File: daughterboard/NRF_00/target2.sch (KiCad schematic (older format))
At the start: 4 parts

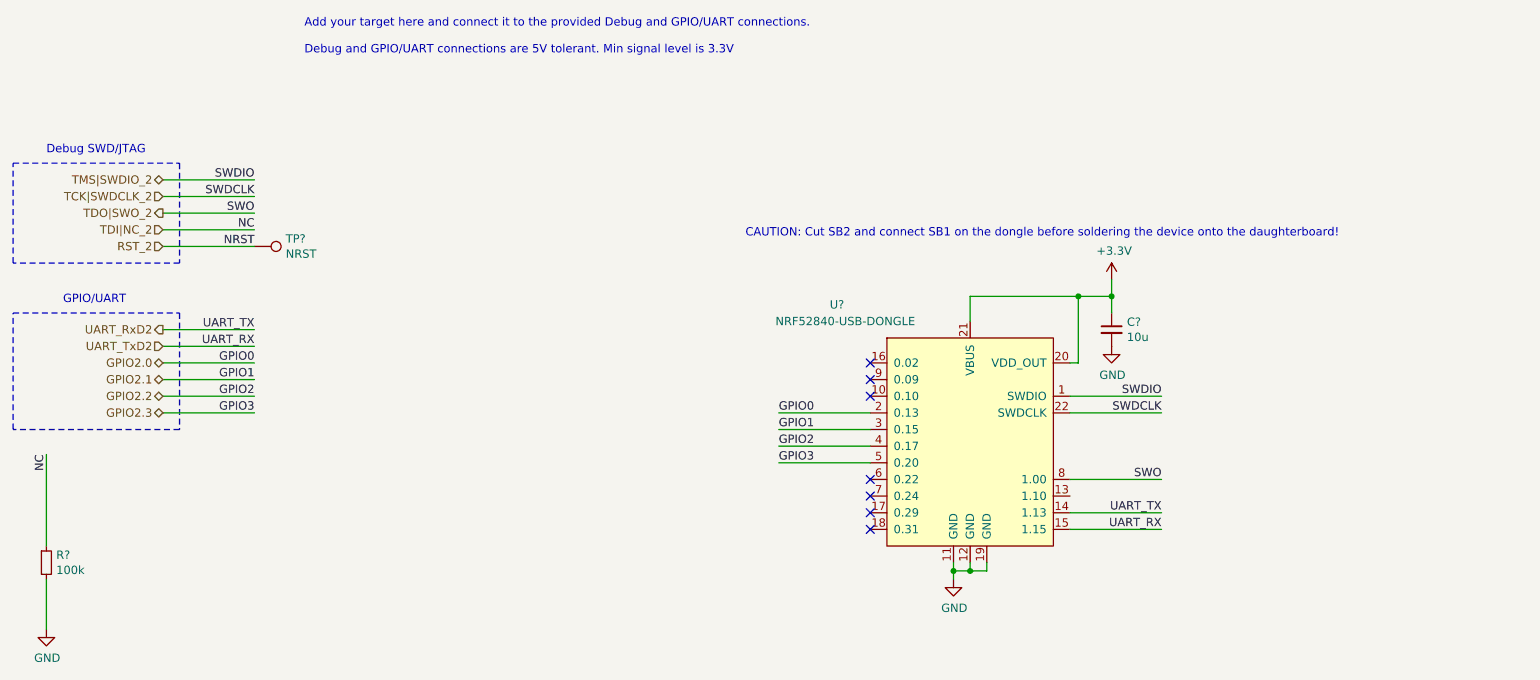
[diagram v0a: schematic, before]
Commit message: finished NRF daughterboard schematics
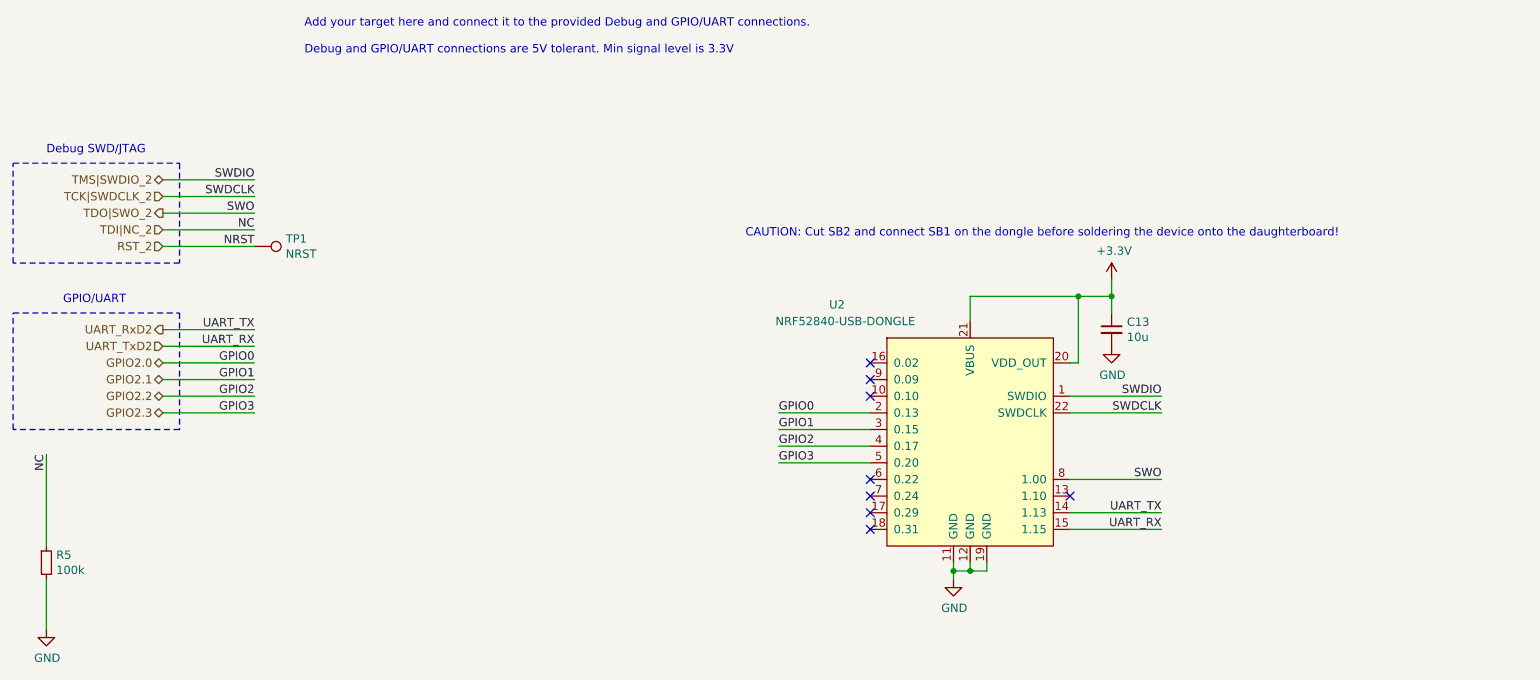
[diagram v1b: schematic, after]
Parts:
- gave numbers to parts that had none: 4
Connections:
- no-connect marks 7 -> 8
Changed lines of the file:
@@
 Add your target here and connect it to the provided Debug and GPIO/UART connections.\n\nDebug and GPIO/UART connections are 5V tolerant. Min signal level is 3.3V
 $Comp
-L hive_daughterboard:NRF52840-USB-DONGLE U?
+L hive_daughterboard:NRF52840-USB-DONGLE U2
 U 1 1 618F653D
 P 6500 2650
-F 0 "U?" H 5700 2850 50  0000 C CNN
+F 0 "U2" H 5700 2850 50  0000 C CNN
 F 1 "NRF52840-USB-DONGLE" H 5750 2750 50  0000 C CNN
 F 2 "hive_daughterboard:NRF52840-USB-DONGLE" H 6500 2650 50  0001 C CNN
@@
 	7150 2800 7100 2800
 $Comp
-L Device:C_Small C?
+L Device:C_Small C13
 U 1 1 618F9760
 P 7350 2600
-F 0 "C?" H 7442 2646 50  0000 L CNN
+F 0 "C13" H 7442 2646 50  0000 L CNN
 F 1 "10u" H 7442 2555 50  0000 L CNN
 F 2 "" H 7350 2600 50  0001 C CNN
@@
 Connection ~ 7150 2400
 $Comp
-L power:GND #PWR?
+L power:GND #PWR017
 U 1 1 618FA4AD
 P 7350 2700
-F 0 "#PWR?" H 7350 2450 50  0001 C CNN
+F 0 "#PWR017" H 7350 2450 50  0001 C CNN
 F 1 "GND" H 7355 2527 50  0000 C CNN
 F 2 "" H 7350 2700 50  0001 C CNN
@@
 $EndComp
 $Comp
-L power:+3.3V #PWR?
+L power:+3.3V #PWR016
 U 1 1 618FB271
 P 7350 2300
-F 0 "#PWR?" H 7350 2150 50  0001 C CNN
+F 0 "#PWR016" H 7350 2150 50  0001 C CNN
 F 1 "+3.3V" H 7365 2473 50  0000 C CNN
 F 2 "" H 7350 2300 50  0001 C CNN
@@
 Connection ~ 7350 2400
 $Comp
-L power:GND #PWR?
+L power:GND #PWR015
 U 1 1 618FC319
 P 6400 4100
-F 0 "#PWR?" H 6400 3850 50  0001 C CNN
+F 0 "#PWR015" H 6400 3850 50  0001 C CNN
 F 1 "GND" H 6405 3927 50  0000 C CNN
 F 2 "" H 6400 4100 50  0001 C CNN
@@
 NC
 $Comp
-L Device:R_Small R?
+L Device:R_Small R5
 U 1 1 619010C0
 P 950 4000
-F 0 "R?" H 1009 4046 50  0000 L CNN
+F 0 "R5" H 1009 4046 50  0000 L CNN
 F 1 "100k" H 1009 3955 50  0000 L CNN
 F 2 "" H 950 4000 50  0001 C CNN
@@
 $EndComp
 $Comp
-L power:GND #PWR?
+L power:GND #PWR014
 U 1 1 61901CB3
 P 950 4400
-F 0 "#PWR?" H 950 4150 50  0001 C CNN
+F 0 "#PWR014" H 950 4150 50  0001 C CNN
 F 1 "GND" H 955 4227 50  0000 C CNN
 F 2 "" H 950 4400 50  0001 C CNN
@@
 	950  4400 950  4100
 $Comp
-L Connector:TestPoint TP?
+L Connector:TestPoint TP1
 U 1 1 61903134
 P 2200 2100
-F 0 "TP?" V 2154 2288 50  0000 L CNN
+F 0 "TP1" V 2154 2288 50  0000 L CNN
 F 1 "NRST" V 2245 2288 50  0000 L CNN
 F 2 "" H 2400 2100 50  0001 C CNN
@@
 NoConn ~ 5900 3700
 NoConn ~ 5900 3800
+NoConn ~ 7100 3600
 $EndSCHEMATC

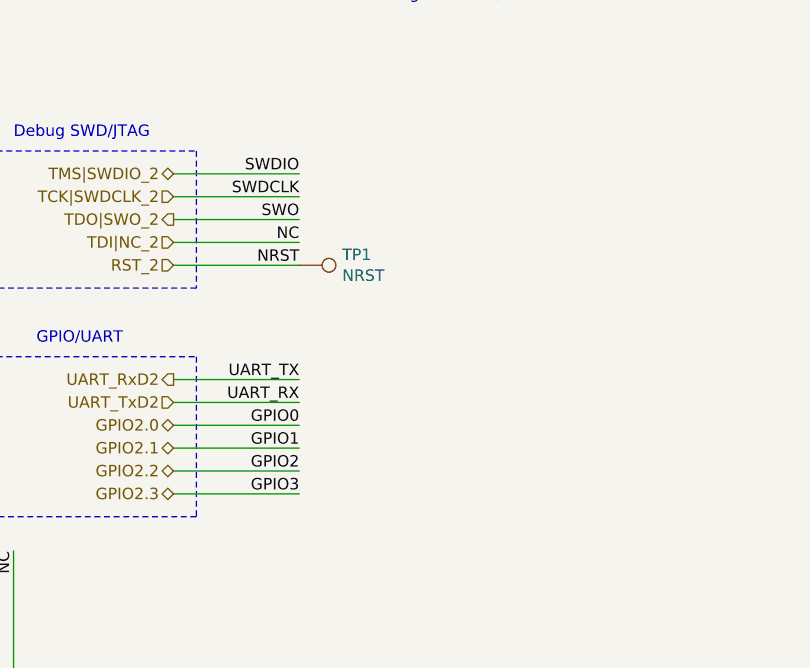
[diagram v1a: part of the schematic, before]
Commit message: added testpoints to daughterboards, updated readme
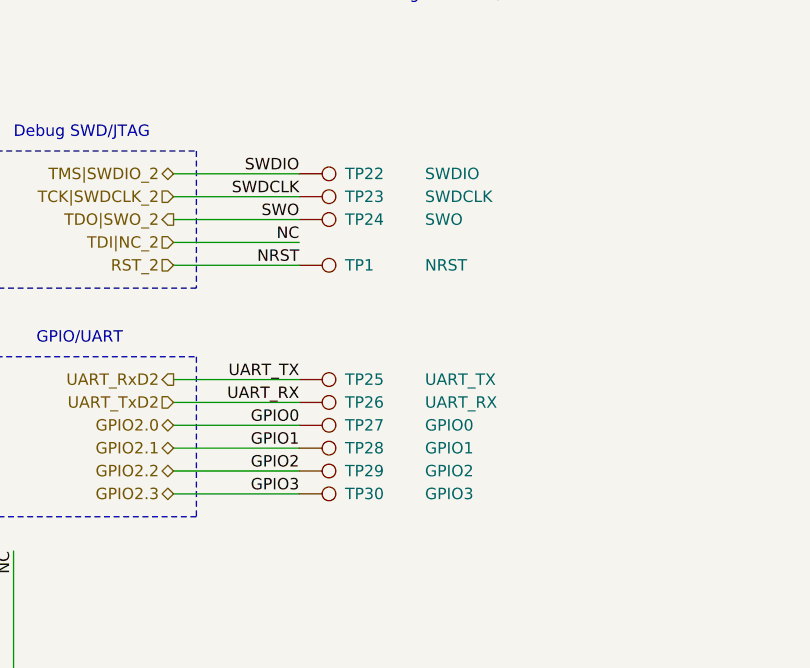
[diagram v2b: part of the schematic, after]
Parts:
- added TP22: SWDIO, symbol Connector:TestPoint
- added TP23: SWDCLK, symbol Connector:TestPoint
- added TP24: SWO, symbol Connector:TestPoint
- added TP25: UART_TX, symbol Connector:TestPoint
- added TP26: UART_RX, symbol Connector:TestPoint
- added TP27: GPIO0, symbol Connector:TestPoint
- added TP28: GPIO1, symbol Connector:TestPoint
- added TP29: GPIO2, symbol Connector:TestPoint
- added TP30: GPIO3, symbol Connector:TestPoint
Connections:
- net GPIO2.0: now also TP27.1
- net GPIO2.1: now also TP28.1
- net GPIO2.2: now also TP29.1
- net GPIO2.3: now also TP30.1
- net TCK|SWDCLK_2: now also TP23.1
- net TDO|SWO_2: now also TP24.1
- net TMS|SWDIO_2: now also TP22.1
- net UART_RxD2: now also TP25.1
- net UART_TxD2: now also TP26.1
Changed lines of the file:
@@
 U 1 1 61903134
 P 2200 2100
-F 0 "TP1" V 2154 2288 50  0000 L CNN
-F 1 "NRST" V 2245 2288 50  0000 L CNN
+F 0 "TP1" V 2200 2300 50  0000 L CNN
+F 1 "NRST" V 2200 2650 50  0000 L CNN
 F 2 "" H 2400 2100 50  0001 C CNN
 F 3 "~" H 2400 2100 50  0001 C CNN
@@
 NoConn ~ 5900 3800
 NoConn ~ 7100 3600
+$Comp
+L Connector:TestPoint TP24
+U 1 1 619068FD
+P 2200 1900
+F 0 "TP24" V 2200 2100 50  0000 L CNN
+F 1 "SWO" V 2200 2450 50  0000 L CNN
+F 2 "" H 2400 1900 50  0001 C CNN
+F 3 "~" H 2400 1900 50  0001 C CNN
+	1    2200 1900
+	0    1    1    0
+$EndComp
+$Comp
+L Connector:TestPoint TP23
+U 1 1 61906DB8
+P 2200 1800
+F 0 "TP23" V 2200 2000 50  0000 L CNN
+F 1 "SWDCLK" V 2200 2350 50  0000 L CNN
+F 2 "" H 2400 1800 50  0001 C CNN
+F 3 "~" H 2400 1800 50  0001 C CNN
+	1    2200 1800
+	0    1    1    0
+$EndComp
+$Comp
+L Connector:TestPoint TP22
+U 1 1 61907190
+P 2200 1700
+F 0 "TP22" V 2200 1900 50  0000 L CNN
+F 1 "SWDIO" V 2200 2250 50  0000 L CNN
+F 2 "" H 2400 1700 50  0001 C CNN
+F 3 "~" H 2400 1700 50  0001 C CNN
+	1    2200 1700
+	0    1    1    0
+$EndComp
+$Comp
+L Connector:TestPoint TP25
+U 1 1 619074D8
+P 2200 2600
+F 0 "TP25" V 2200 2800 50  0000 L CNN
+F 1 "UART_TX" V 2200 3150 50  0000 L CNN
+F 2 "" H 2400 2600 50  0001 C CNN
+F 3 "~" H 2400 2600 50  0001 C CNN
+	1    2200 2600
+	0    1    1    0
+$EndComp
+$Comp
+L Connector:TestPoint TP26
+U 1 1 61907EED
+P 2200 2700
+F 0 "TP26" V 2200 2900 50  0000 L CNN
+F 1 "UART_RX" V 2200 3250 50  0000 L CNN
+F 2 "" H 2400 2700 50  0001 C CNN
+F 3 "~" H 2400 2700 50  0001 C CNN
+	1    2200 2700
+	0    1    1    0
+$EndComp
+$Comp
+L Connector:TestPoint TP27
+U 1 1 619081A4
+P 2200 2800
+F 0 "TP27" V 2200 3000 50  0000 L CNN
+F 1 "GPIO0" V 2200 3350 50  0000 L CNN
+F 2 "" H 2400 2800 50  0001 C CNN
+F 3 "~" H 2400 2800 50  0001 C CNN
+	1    2200 2800
+	0    1    1    0
+$EndComp
+$Comp
+L Connector:TestPoint TP28
+U 1 1 6190853B
+P 2200 2900
+F 0 "TP28" V 2200 3100 50  0000 L CNN
+F 1 "GPIO1" V 2200 3450 50  0000 L CNN
+F 2 "" H 2400 2900 50  0001 C CNN
+F 3 "~" H 2400 2900 50  0001 C CNN
+	1    2200 2900
+	0    1    1    0
+$EndComp
+$Comp
+L Connector:TestPoint TP29
+U 1 1 61908837
+P 2200 3000
+F 0 "TP29" V 2200 3200 50  0000 L CNN
+F 1 "GPIO2" V 2200 3550 50  0000 L CNN
+F 2 "" H 2400 3000 50  0001 C CNN
+F 3 "~" H 2400 3000 50  0001 C CNN
+	1    2200 3000
+	0    1    1    0
+$EndComp
+$Comp
+L Connector:TestPoint TP30
+U 1 1 61908AC3
+P 2200 3100
+F 0 "TP30" V 2200 3300 50  0000 L CNN
+F 1 "GPIO3" V 2200 3650 50  0000 L CNN
+F 2 "" H 2400 3100 50  0001 C CNN
+F 3 "~" H 2400 3100 50  0001 C CNN
+	1    2200 3100
+	0    1    1    0
+$EndComp
 $EndSCHEMATC

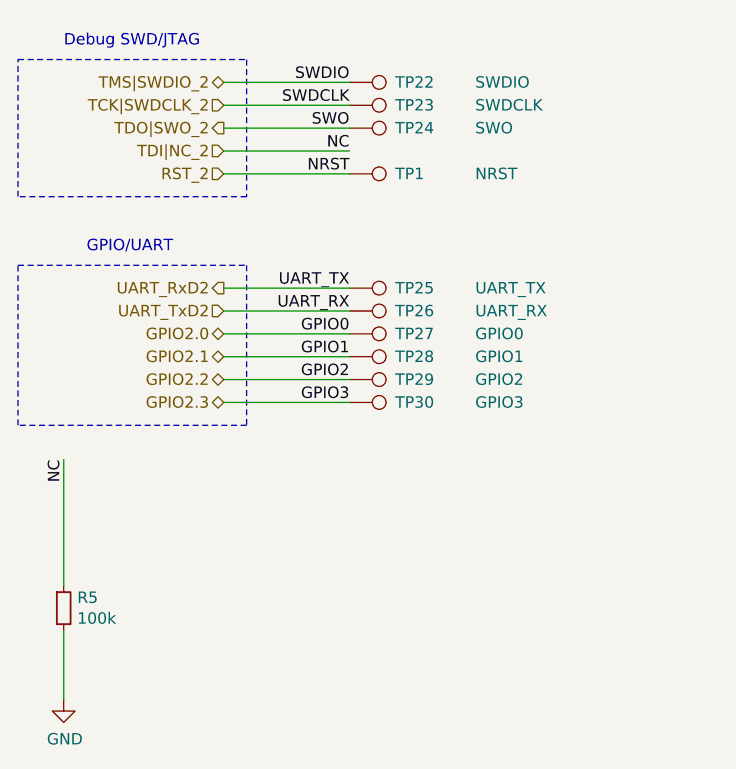
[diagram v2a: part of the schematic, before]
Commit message: finished NRF daughterboard layout
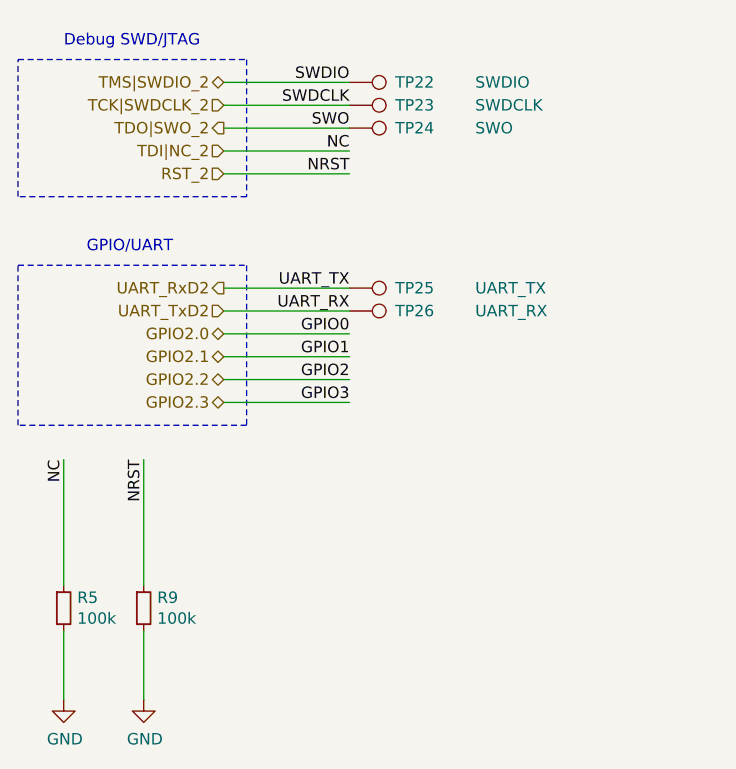
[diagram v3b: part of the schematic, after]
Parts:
- removed TP1: NRST, symbol Connector:TestPoint
- removed TP27: GPIO0, symbol Connector:TestPoint
- removed TP28: GPIO1, symbol Connector:TestPoint
- removed TP29: GPIO2, symbol Connector:TestPoint
- removed TP30: GPIO3, symbol Connector:TestPoint
- added R9: 100k, Resistor_SMD:R_0603_1608Metric_Pad1.05x0.95mm_HandSolder, symbol Device:R_Small
- C13: footprint (none) -> Capacitor_SMD:C_0603_1608Metric_Pad1.05x0.95mm_HandSolder
- R5: footprint (none) -> Resistor_SMD:R_0603_1608Metric_Pad1.05x0.95mm_HandSolder
- TP22, TP23, TP24, TP25, TP26: footprint (none) -> TestPoint:TestPoint_Pad_1.0x1.0mm
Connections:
- net GND: now also R9.2
- net RST_2: now also R9.1
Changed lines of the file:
@@
 F 0 "C13" H 7442 2646 50  0000 L CNN
 F 1 "10u" H 7442 2555 50  0000 L CNN
-F 2 "" H 7350 2600 50  0001 C CNN
+F 2 "Capacitor_SMD:C_0603_1608Metric_Pad1.05x0.95mm_HandSolder" H 7350 2600 50  0001 C CNN
 F 3 "~" H 7350 2600 50  0001 C CNN
 	1    7350 2600
@@
 F 0 "R5" H 1009 4046 50  0000 L CNN
 F 1 "100k" H 1009 3955 50  0000 L CNN
-F 2 "" H 950 4000 50  0001 C CNN
+F 2 "Resistor_SMD:R_0603_1608Metric_Pad1.05x0.95mm_HandSolder" H 950 4000 50  0001 C CNN
 F 3 "~" H 950 4000 50  0001 C CNN
 	1    950  4000
@@
 Wire Wire Line
 	950  4400 950  4100
-$Comp
-L Connector:TestPoint TP1
-U 1 1 61903134
-P 2200 2100
-F 0 "TP1" V 2200 2300 50  0000 L CNN
-F 1 "NRST" V 2200 2650 50  0000 L CNN
-F 2 "" H 2400 2100 50  0001 C CNN
-F 3 "~" H 2400 2100 50  0001 C CNN
-	1    2200 2100
-	0    1    1    0
-$EndComp
 Wire Wire Line
 	7100 3700 7650 3700
@@
 F 0 "TP24" V 2200 2100 50  0000 L CNN
 F 1 "SWO" V 2200 2450 50  0000 L CNN
-F 2 "" H 2400 1900 50  0001 C CNN
+F 2 "TestPoint:TestPoint_Pad_1.0x1.0mm" H 2400 1900 50  0001 C CNN
 F 3 "~" H 2400 1900 50  0001 C CNN
 	1    2200 1900
@@
 F 0 "TP23" V 2200 2000 50  0000 L CNN
 F 1 "SWDCLK" V 2200 2350 50  0000 L CNN
-F 2 "" H 2400 1800 50  0001 C CNN
+F 2 "TestPoint:TestPoint_Pad_1.0x1.0mm" H 2400 1800 50  0001 C CNN
 F 3 "~" H 2400 1800 50  0001 C CNN
 	1    2200 1800
@@
 F 0 "TP22" V 2200 1900 50  0000 L CNN
 F 1 "SWDIO" V 2200 2250 50  0000 L CNN
-F 2 "" H 2400 1700 50  0001 C CNN
+F 2 "TestPoint:TestPoint_Pad_1.0x1.0mm" H 2400 1700 50  0001 C CNN
 F 3 "~" H 2400 1700 50  0001 C CNN
 	1    2200 1700
@@
 F 0 "TP25" V 2200 2800 50  0000 L CNN
 F 1 "UART_TX" V 2200 3150 50  0000 L CNN
-F 2 "" H 2400 2600 50  0001 C CNN
+F 2 "TestPoint:TestPoint_Pad_1.0x1.0mm" H 2400 2600 50  0001 C CNN
 F 3 "~" H 2400 2600 50  0001 C CNN
 	1    2200 2600
@@
 F 0 "TP26" V 2200 2900 50  0000 L CNN
 F 1 "UART_RX" V 2200 3250 50  0000 L CNN
-F 2 "" H 2400 2700 50  0001 C CNN
+F 2 "TestPoint:TestPoint_Pad_1.0x1.0mm" H 2400 2700 50  0001 C CNN
 F 3 "~" H 2400 2700 50  0001 C CNN
 	1    2200 2700
 	0    1    1    0
 $EndComp
-$Comp
-L Connector:TestPoint TP27
-U 1 1 619081A4
-P 2200 2800
-F 0 "TP27" V 2200 3000 50  0000 L CNN
-F 1 "GPIO0" V 2200 3350 50  0000 L CNN
-F 2 "" H 2400 2800 50  0001 C CNN
-F 3 "~" H 2400 2800 50  0001 C CNN
-	1    2200 2800
-	0    1    1    0
-$EndComp
-$Comp
-L Connector:TestPoint TP28
-U 1 1 6190853B
-P 2200 2900
-F 0 "TP28" V 2200 3100 50  0000 L CNN
-F 1 "GPIO1" V 2200 3450 50  0000 L CNN
-F 2 "" H 2400 2900 50  0001 C CNN
-F 3 "~" H 2400 2900 50  0001 C CNN
-	1    2200 2900
-	0    1    1    0
-$EndComp
-$Comp
-L Connector:TestPoint TP29
-U 1 1 61908837
-P 2200 3000
-F 0 "TP29" V 2200 3200 50  0000 L CNN
-F 1 "GPIO2" V 2200 3550 50  0000 L CNN
-F 2 "" H 2400 3000 50  0001 C CNN
-F 3 "~" H 2400 3000 50  0001 C CNN
-	1    2200 3000
-	0    1    1    0
-$EndComp
-$Comp
-L Connector:TestPoint TP30
-U 1 1 61908AC3
-P 2200 3100
-F 0 "TP30" V 2200 3300 50  0000 L CNN
-F 1 "GPIO3" V 2200 3650 50  0000 L CNN
-F 2 "" H 2400 3100 50  0001 C CNN
-F 3 "~" H 2400 3100 50  0001 C CNN
-	1    2200 3100
-	0    1    1    0
-$EndComp
+Wire Wire Line
+	1300 3900 1300 3350
+Text Label 1300 3350 3    50   ~ 0
+NRST
+$Comp
+L Device:R_Small R9
+U 1 1 6195C66B
+P 1300 4000
+F 0 "R9" H 1359 4046 50  0000 L CNN
+F 1 "100k" H 1359 3955 50  0000 L CNN
+F 2 "Resistor_SMD:R_0603_1608Metric_Pad1.05x0.95mm_HandSolder" H 1300 4000 50  0001 C CNN
+F 3 "~" H 1300 4000 50  0001 C CNN
+	1    1300 4000
+	1    0    0    -1
+$EndComp
+$Comp
+L power:GND #PWR025
+U 1 1 6195C671
+P 1300 4400
+F 0 "#PWR025" H 1300 4150 50  0001 C CNN
+F 1 "GND" H 1305 4227 50  0000 C CNN
+F 2 "" H 1300 4400 50  0001 C CNN
+F 3 "" H 1300 4400 50  0001 C CNN
+	1    1300 4400
+	1    0    0    -1
+$EndComp
+Wire Wire Line
+	1300 4400 1300 4100
 $EndSCHEMATC
